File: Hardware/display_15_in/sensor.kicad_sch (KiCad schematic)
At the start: 16 parts

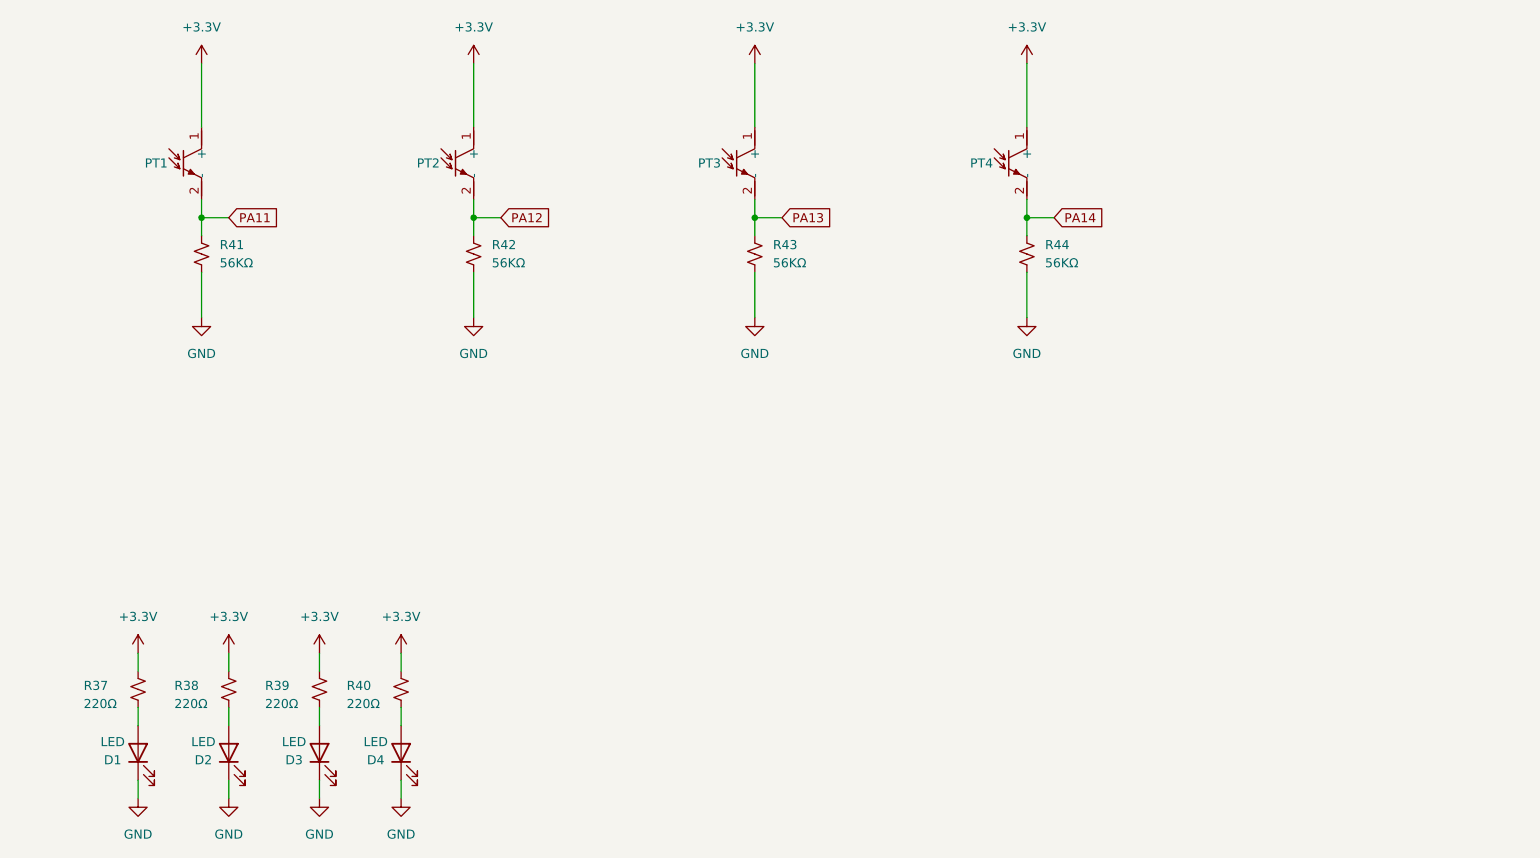
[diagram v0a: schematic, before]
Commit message: routed more traces
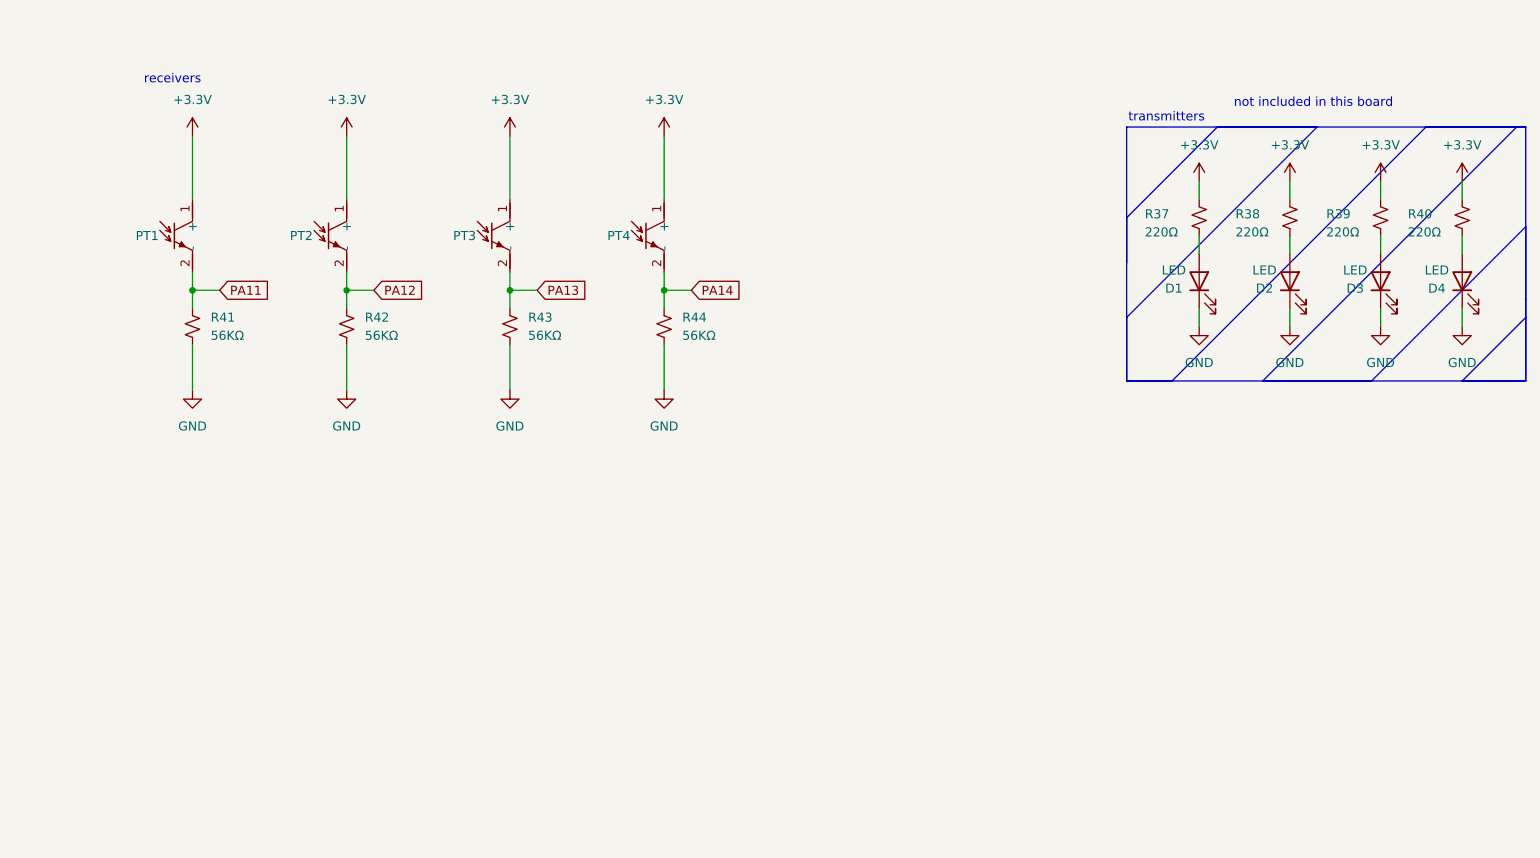
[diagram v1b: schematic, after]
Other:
- note added: "not included in this board"
- note added: "receivers"
- note added: "transmitters"
- title: (none) -> IR_sensor_receivers
- moved on the sheet: D1, D2, D3, D4, PT1, PT2, PT3, PT4, R37, R38, R39, R40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

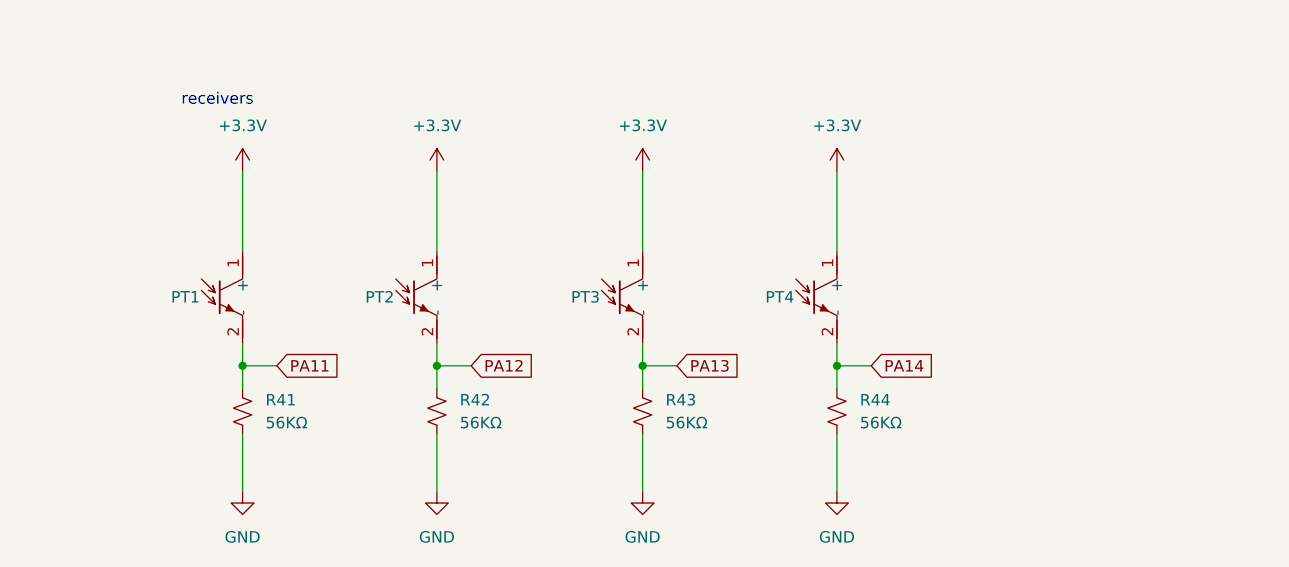
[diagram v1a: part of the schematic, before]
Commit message: power traces, gnd plane vias, and test points
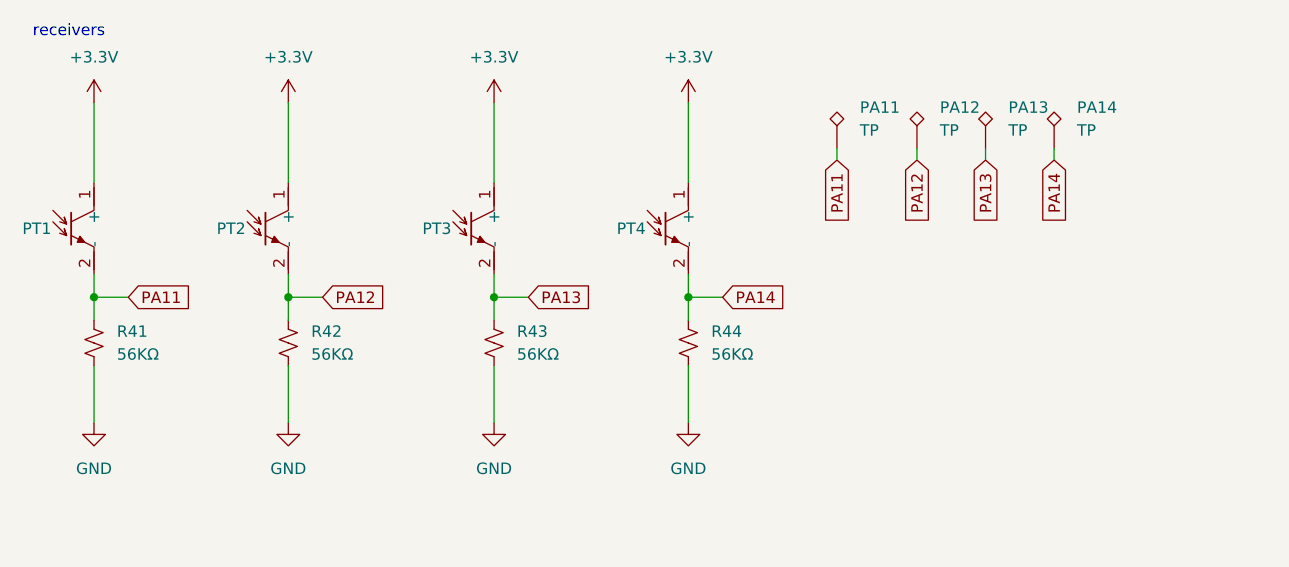
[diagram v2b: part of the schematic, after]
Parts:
- added PA11, PA12, PA13, PA14: TP, TestPoint:TestPoint_Keystone_5019_Minature, symbol Connector:TestPoint_Alt
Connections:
- net PA11: now also PA11.1
- net PA12: now also PA12.1
- net PA13: now also PA13.1
- net PA14: now also PA14.1
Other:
- moved on the sheet: PT1, PT2, PT3, PT4, R41, R42, R43, R44
